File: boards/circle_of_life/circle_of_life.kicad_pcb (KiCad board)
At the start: 2 copper layers, 87.4 x 96.4 mm, 120 parts, among them IC1 ESP32-WROOM-32E-N8R2, IC2 TC1262-3.3VDB, IC3 TPS565242DRLR, IC4 LT3922EUFD#PBF, IC5 TXU0101DBVR, IC6 CP2102C-A01-GQFN28, J1 Water Pump Connector, J11 LED Connector, J2 Servo Motor Connector, J3 Power Connector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

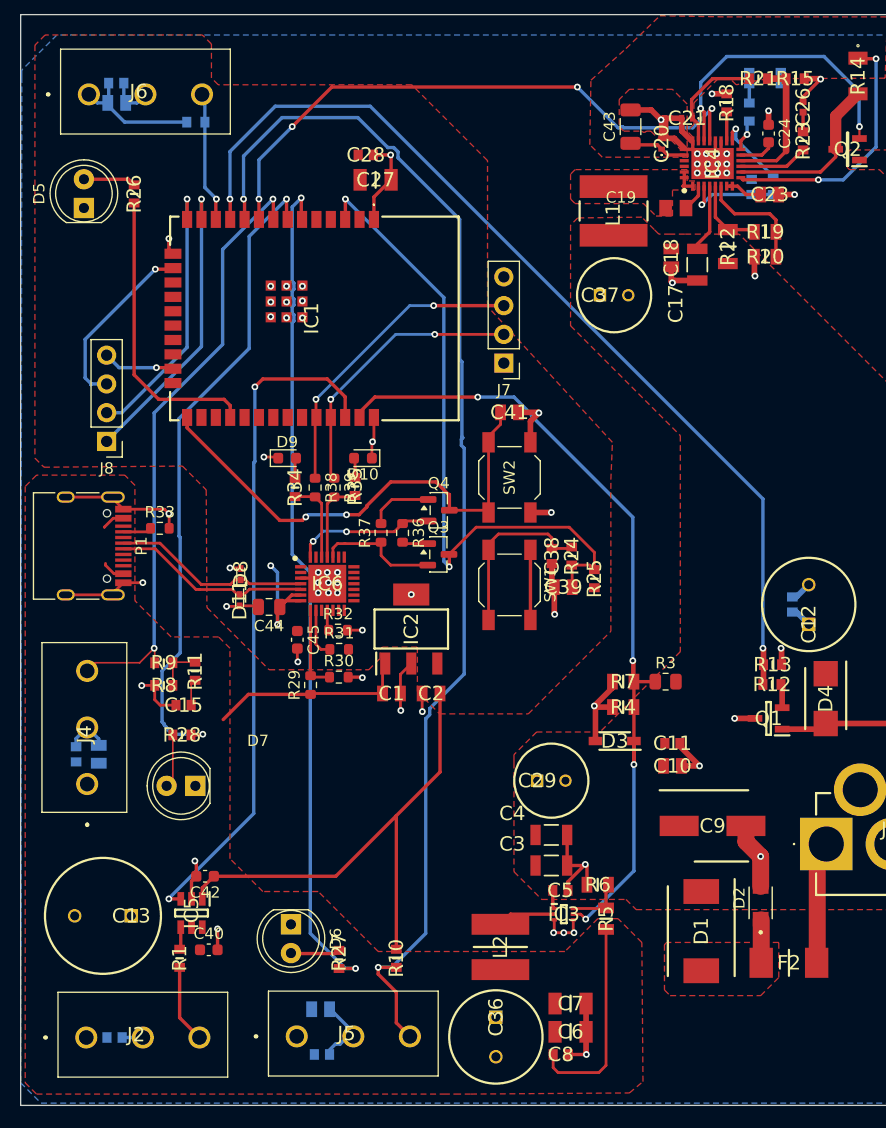
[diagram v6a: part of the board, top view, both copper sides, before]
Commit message: fixed some footprints
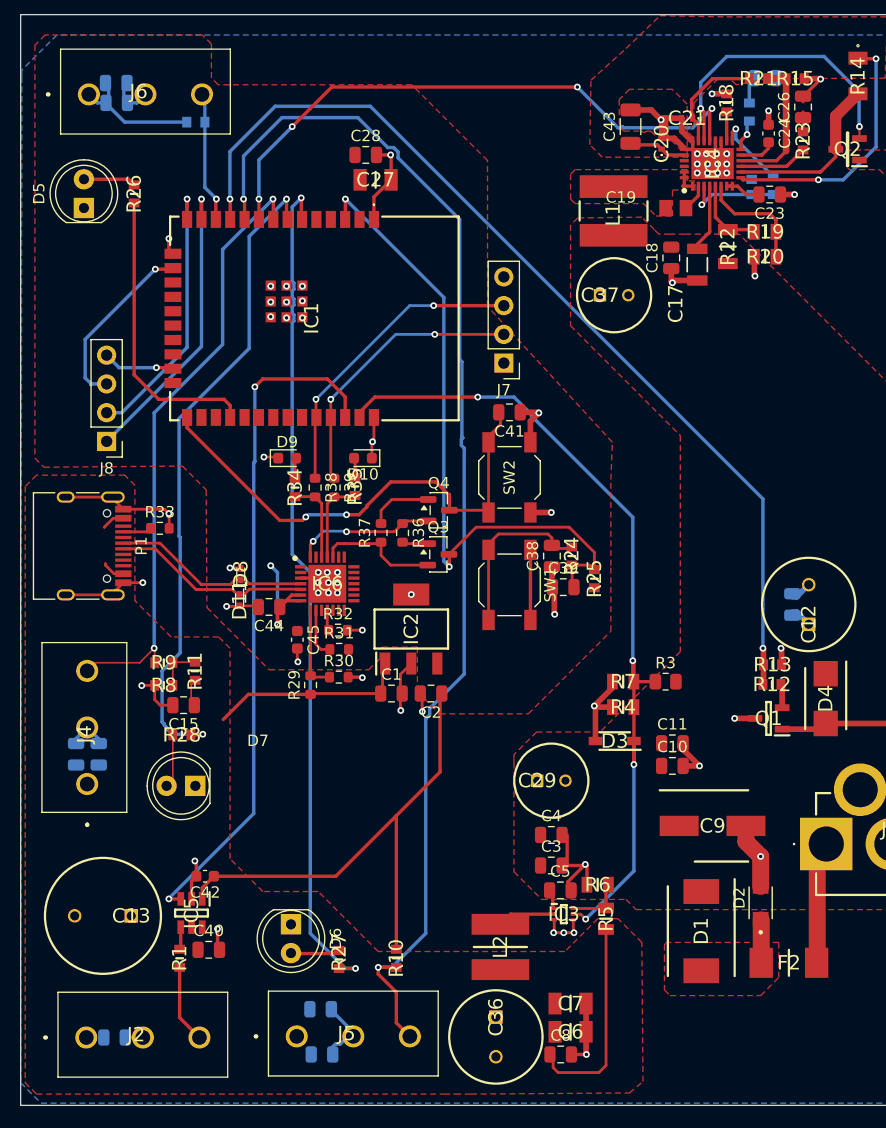
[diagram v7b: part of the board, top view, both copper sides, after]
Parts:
- C1, C10, C18, C2, C23, C30, C33, C35, C39, C41: footprint SamacSys_Parts:CAPC2012X135N -> Capacitor_SMD:C_0805_2012Metric
- C11, C14, C15, C16, C28, C31, C32, C34, C38, C5, C8: footprint SamacSys_Parts:CAPC1608X90N -> Capacitor_SMD:C_0805_2012Metric
- C25, C3, C4: footprint SamacSys_Parts:CAPC3216X180N -> Capacitor_SMD:C_0805_2012Metric
- C26: footprint SamacSys_Parts:CAPC1005X70N -> Capacitor_SMD:C_0805_2012Metric
- C40: footprint Capacitor_SMD:C_0603_1608Metric -> Capacitor_SMD:C_0805_2012Metric

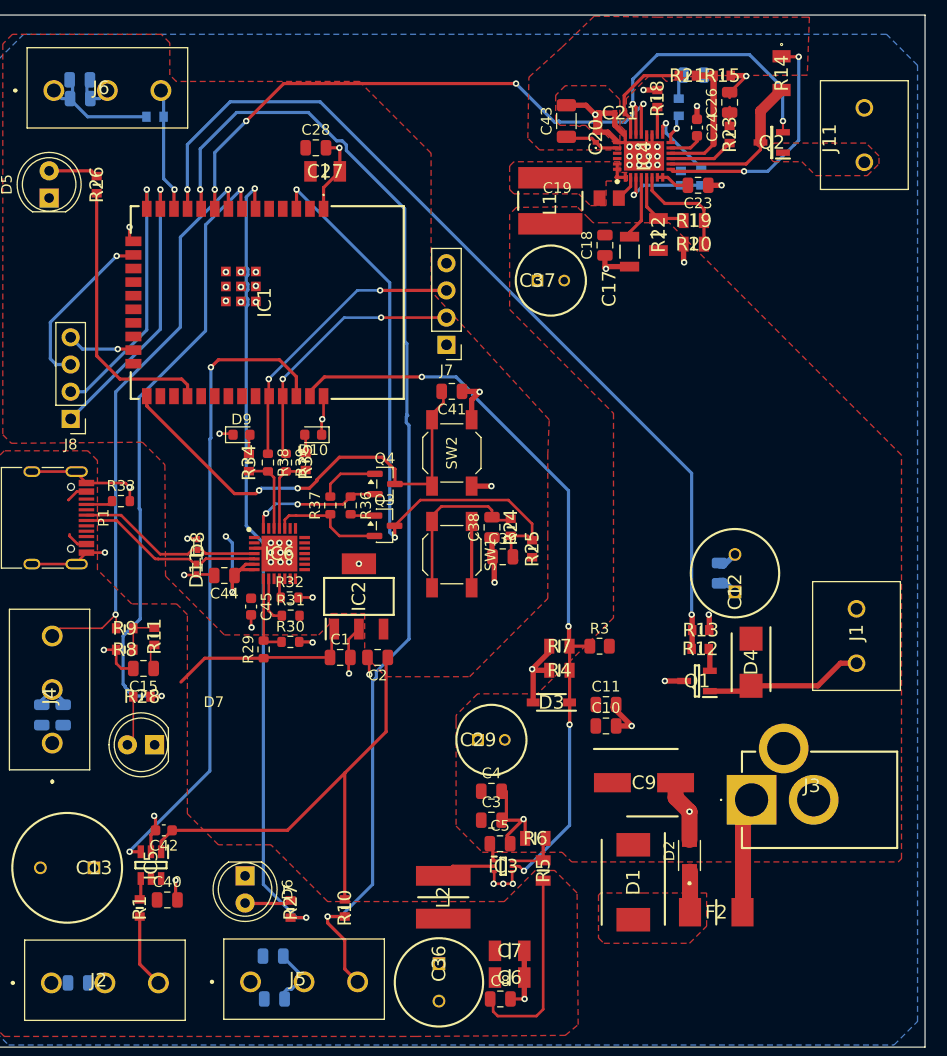
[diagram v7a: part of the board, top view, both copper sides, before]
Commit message: fixed most of the footprints errors
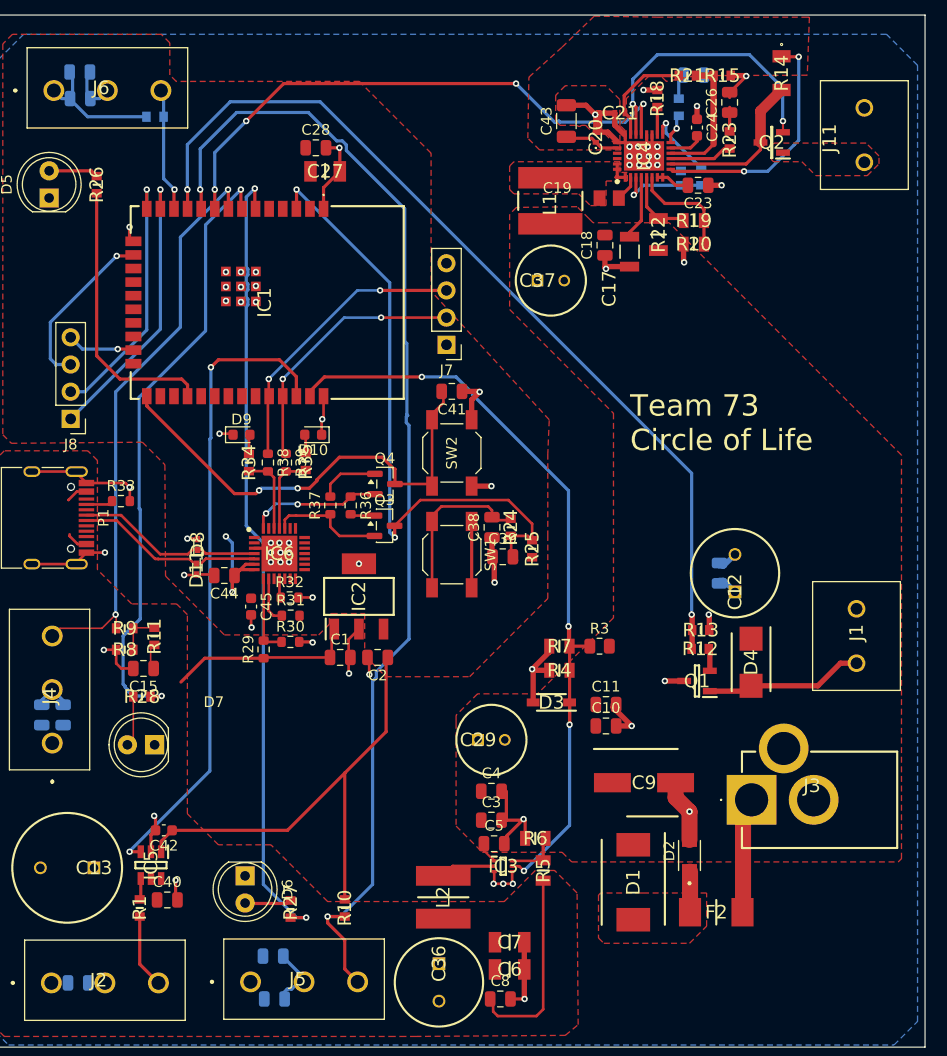
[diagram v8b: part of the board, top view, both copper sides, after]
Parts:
- moved C7 0.80 mm to (134.8, 190.5)
- moved C6 0.76 mm to (134.8, 193.0)
- moved C34 0.73 mm to (94.7, 109.2)
- moved C5 0.55 mm to (133.3, 181.3)
- moved R23 0.51 mm to (155.3, 115.6)
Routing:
- net GND: track 149.1 -> 150.0 mm
- net +3.3V: track 68.3 -> 69.1 mm
- net +12V: track 9.55 -> 10.1 mm
- net Net-(C26-Pad1): track 1.74 -> 2.25 mm
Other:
- board text added: "Team 73 Circle of Life"
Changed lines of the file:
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@@
 			(outputformat 1)
 			(mirror no)
-			(drillshape 1)
+			(drillshape 0)
 			(scaleselection 1)
 			(outputdirectory "")
@@
 	(footprint "Capacitor_SMD:C_0805_2012Metric"
 		(layer "F.Cu")
-		(at 133.9 181.3)
+		(at 133.35 181.3)
 		(descr "Capacitor SMD 0805 (2012 Metric), square (rectangular) end terminal, IPC-7351 nominal, (Body size source: IPC-SM-782 page 76, https://www.pcb-3d.com/wordpress/wp-content/uploads/ipc-sm-782a_amendment_1_and_2.pdf, https://docs.google.com/spreadsheets/d/1BsfQQcO9C6DZCsRaXUlFlo91Tg2WpOkGARC1WS5S8t0/edit?usp=sharing), generated with kicad-footprint-generator")
 		(tags "capacitor")
@@
 	(footprint "SamacSys_Parts:RESC1608X55N"
 		(layer "F.Cu")
-		(at 155.35 115.06 -90)
+		(at 155.35 115.57 -90)
 		(descr "RC0603")
 		(tags "Resistor")
@@
 	(footprint "SamacSys_Parts:CAPC3216X190N"
 		(layer "F.Cu")
-		(at 134.8 193.8)
+		(at 134.8 193.04)
 		(descr "3.2X1.6_2021")
 		(tags "Capacitor")
@@
 	(footprint "SamacSys_Parts:CAPC3216X190N"
 		(layer "F.Cu")
-		(at 134.8 191.3)
+		(at 134.8 190.5)
 		(descr "3.2X1.6_2021")
 		(tags "Capacitor")
@@
 	(footprint "Capacitor_SMD:C_0805_2012Metric"
 		(layer "B.Cu")
-		(at 94.65 109.95)
+		(at 94.65 109.22)
 		(descr "Capacitor SMD 0805 (2012 Metric), square (rectangular) end terminal, IPC-7351 nominal, (Body size source: IPC-SM-782 page 76, https://www.pcb-3d.com/wordpress/wp-content/uploads/ipc-sm-782a_amendment_1_and_2.pdf, https://docs.google.com/spreadsheets/d/1BsfQQcO9C6DZCsRaXUlFlo91Tg2WpOkGARC1WS5S8t0/edit?usp=sharing), generated with kicad-footprint-generator")
 		(tags "capacitor")
@@
 		(layer "Edge.Cuts")
 	)
+	(gr_text "Team 73\nCircle of Life"
+		(at 146.05 144.78 0)
+		(layer "F.SilkS")
+		(effects
+			(font
+				(size 2 2)
+				(thickness 0.2)
+			)
+			(justify left bottom)
+		)
+	)
 	(segment
 		(start 144.625 113.06)
@@
 	)
 	(segment
+		(start 134.57 180.53)
+		(end 134.57 181.03)
+		(width 0.3)
+		(layer "F.Cu")
+		(net 1)
+	)
+	(segment
 		(start 143.7 126.19)
 		(end 143.7 127.5)
@@
 	)
 	(segment
+		(start 134.57 181.03)
+		(end 134.3 181.3)
+		(width 0.3)
+		(layer "F.Cu")
+		(net 1)
+	)
+	(segment
 		(start 99.325 149.3)
 		(end 99.325 148.025)
@@
 	)
 	(segment
-		(start 93.98 109.95)
-		(end 93.98 111.62)
+		(start 93.98 109.5)
+		(end 93.7 109.22)
 		(width 0.3)
 		(layer "B.Cu")
@@
 	)
 	(segment
-		(start 108.9 157.8)
-		(end 108.9 153.2)
+		(start 93.98 111.62)
+		(end 93.98 109.5)
 		(width 0.3)
 		(layer "B.Cu")
@@
 	)
 	(segment
-		(start 93.98 111.62)
-		(end 93.9 111.7)
+		(start 108.9 157.8)
+		(end 108.9 153.2)
 		(width 0.3)
 		(layer "B.Cu")
@@
 	)
 	(segment
+		(start 93.9 111.7)
+		(end 93.98 111.62)
+		(width 0.3)
+		(layer "B.Cu")
+		(net 3)
+	)
+	(segment
 		(start 108.9 153.2)
 		(end 108.3 152.6)
@@
 	)
 	(segment
+		(start 132.4 181.3)
+		(end 132.4 181.938)
+		(width 0.2)
+		(layer "F.Cu")
+		(net 4)
+	)
+	(segment
 		(start 147.1 123.1)
 		(end 146 124.2)
@@
 	)
 	(segment
-		(start 146 124.2)
-		(end 146 124.603)
-		(width 0.3)
+		(start 132.4 181.938)
+		(end 133.362 182.9)
+		(width 0.2)
 		(layer "F.Cu")
 		(net 4)
 	)
 	(segment
-		(start 133.23 181.3)
-		(end 133.23 182.768)
+		(start 146 124.2)
+		(end 146 124.603)
 		(width 0.3)
 		(layer "F.Cu")
@@
 	)
 	(segment
-		(start 155.35 114.26)
-		(end 155.35 112.52)
+		(start 155.35 112.52)
+		(end 155.35 114.77)
 		(width 0.3)
 		(layer "F.Cu")
@@
 	)
 	(segment
-		(start 153.9 117.31)
-		(end 155.35 115.86)
+		(start 154.84 116.37)
+		(end 155.35 116.37)
+		(width 0.2)
+		(layer "F.Cu")
+		(net 54)
+	)
+	(segment
+		(start 154.84 116.37)
+		(end 153.9 117.31)
 		(width 0.3)
 		(layer "F.Cu")
